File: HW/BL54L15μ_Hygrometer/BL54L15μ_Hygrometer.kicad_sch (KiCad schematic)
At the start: 20 parts, among them IC1 nrf54L 453-00223R, J1 Conn_Qwiic, J2 Conn_ARM_JTAG_SWD_10, J3 Conn_01x10_Pin, J4 Conn_01x10_Pin, J5 Conn_01x10_Pin, J6 Conn_01x10_Pin, U2 nPM2100-QEXX, U3 SHT4x

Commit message: nrf54L hygrometer prototype 2025v2
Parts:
- removed J3, J4, J5, J6: Conn_01x10_Pin, Connector_PinHeader_2.54mm:PinHeader_1x10_P2.54mm_Vertical, symbol Connector:Conn_01x10_Pin
- added C8, C9: 100nF, Capacitor_SMD:C_0402_1005Metric, symbol Device:C
- added U3: STCC4-D-R3, STCC4DR3, symbol STCC4-D-R3:STCC4-D-R3
- added U5: BME688, Package_LGA:Bosch_LGA-8_3x3mm_P0.8mm_ClockwisePinNumbering, symbol Sensor:BME680
- added X1: 32.768 kHz, Crystal:Crystal_SMD_2012-2Pin_2.0x1.2mm, symbol Device:Crystal
- BT1: Digikey Part Number (none) -> 36-2468-ND
- C1: value 47μF -> 22μF; Design Guidance At least 3.5 μF effective and 6.3V rating, ±20% is fine -> (none); Digikey Part Number (none) -> 1276-1274-1-ND
- C2: value 10nF -> 100nF; Design Guidance 1-100nF, at least 6.3V rating -> (none); Digikey Part Number (none) -> 490-6297-1-ND
- C3: Digikey Part Number (none) -> 1276-1192-1-ND
- C4: Digikey Part Number (none) -> 1276-1469-1-ND
- C5: value 10nF -> 100nF; Design Guideline 1-100nF, at least 6.3V rating -> (none); Digikey Part Number (none) -> 490-6297-1-ND
- C6: value 47μF -> 22μF; Design Guideline At least 3.5 μF effective and 6.3V rating, ±20% is fine. Ad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 -> (none); Digikey Part Number (none) -> 1276-1274-1-ND
- C7: Digikey Part Number (none) -> 490-6297-1-ND
- D1: Digikey Part Number (none) -> 732-4979-1-ND
- IC1: Digikey Part Number (none) -> 776-453-00223RCT-ND
- J1: Digikey Part Number (none) -> 455-SM04B-SRSS-TBCT-ND
- J2: Digikey Part Number (none) -> 1528-752-ND
- L1: Digikey Part Number (none) -> 1276-6901-1-ND
- R1: value 2K -> 100Ω; Digikey Part Number (none) -> 311-100HRCT-ND
- U1: renamed from U2; Digikey Part Number (none) -> 4823-NPM2100-QEAA-RCT-ND
- U2: renamed from U3; Digikey Part Number (none) -> 1649-SHT45-AD1F-R2CT-ND
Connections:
- net P1.14 is gone; now on net LED: IC1.18 (P1.14)
- net AVSS2: now also C8.2, C9.2, U3.3 (ADDR), U3.4 (VSS), U5.1 (GND), U5.5 (SDO), U5.7 (GND)
- net GPIO0: now also IC1.1 (P2.05); no longer IC1.8 (P1.07)
- net LED: no longer IC1.1 (P2.05)
- net VDD: now also C7.1, U2.3 (VDD)
- net VDDSW: now also C8.1, C9.1, U3.6 (VDDIO), U3.7 (VDD), U5.2 (CSB), U5.6 (VDDIO), U5.8 (VDD); no longer C7.1, U2.3 (VDD)
- net GPIO1: no longer names the net of U1.9 (GPIO1)
- net GPIO1: no longer IC1.9 (P1.03/NFC2/CLK)
- net P1.00 renamed XL1
- net XL1: now also X1.2
- net P1.02: no longer names the net of IC1.11 (P1.02/NFC1)
- net P1.04 renamed SCL2
- net SCL2: now also J1.4, U3.1 (SCL), U5.4 (SCK)
- net P1.05 renamed SDA2
- net SDA2: now also J1.3, U3.5 (SDA), U5.3 (SDI)
- net P1.08: no longer names the net of IC1.3 (P1.08/EXTREF/CLK16M/CLK)
- net P1.10: no longer names the net of IC1.21 (P1.10)
- net P1.11: no longer names the net of IC1.23 (P1.11/AIN4/CLK)
- net P1.12: no longer names the net of IC1.19 (P1.12/AIN5/CLK)
- net P2.00 renamed SDA1
- net SDA1: now also U1.6 (SDA), U2.1 (SDA)
- net P2.04: no longer names the net of IC1.45 (P2.04)
- net P2.06 renamed SCL1
- net SCL1: now also U1.7 (SCL), U2.2 (SCL)
- net P2.10: no longer names the net of IC1.41 (P2.10)
- net PG/RESET: no longer names the net of U1.10 (PG/RESET)
- net PG/RESET: no longer IC1.10 (P1.01/XL2)
- removed net SCL: IC1.6 (P2.01/CLK), J1.4, U1.7 (SCL), U2.2 (SCL)
- removed net SDA: IC1.7 (P1.06), J1.3, U1.6 (SDA), U2.1 (SDA)
- net SHPHELD: no longer names the net of U1.4 (SHPHLD)
- net SYSGDEN: no longer names the net of U1.8 (SYSGDEN)
- new net XL2: IC1.10 (P1.01/XL2), X1.1
- no-connect marks 15 -> 31
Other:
- note added: "ARM SWD 10-pin header"
- note added: "BL54L15μ (nrf54L15 module)"
- note added: "CO2 STCC4"
- note added: "Humidity/Temperature SHT4X"
- note added: "I2C Address = 0x64 VDD = 2.7 V - 5.5 V 1 μA sleep, 55 μA idle, 3.7 mA peak Accuracy: ±(100 ppm + 10%) (when SHT4x calibrated) 10 year lifetime"
- note added: "I2C Address: 0x44 VDD: 1.08 V - 3.6 V 0.08 μA idle, 320 μA sense, 6-100 mA heat %RH Accuracy: SHT40-43 ±1.8, SHT45 ±1.0 °C Accuracy: SHT40-43 ±0.2, SHT45 ±0.1"
- note added: "I2C Address: 0x74 Vbat: 0.7 - 3.4 V, automatic passthrough Vout: 3V initial (NC Vset), adjustable target 1.8-3.3 V 150 mA boost, 50 mA LDO/switch max output Boost efficiency 87-95% 175 nA hibernate, 35 nA ship mode Fuel gauge, boot watchdog, ADC for VBAT/VOUT/temp"
- note added: "I2C Address: 0x76 VDD: 1.71 V - 3.6 V 0.29 μA idle, 714 μA typ pressure, 12 mA typ gas"
- note added: "Non-rechargable Battery PMIC npm2100"
- note added: "Pressure/Gas BME688"
- note added: "Qwicc I2C Connector"
- note added: "Status LED"
- moved on the sheet: BT1, C1, C2, C3, C4, C5, C6, C7, D1, IC1, J1, J2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

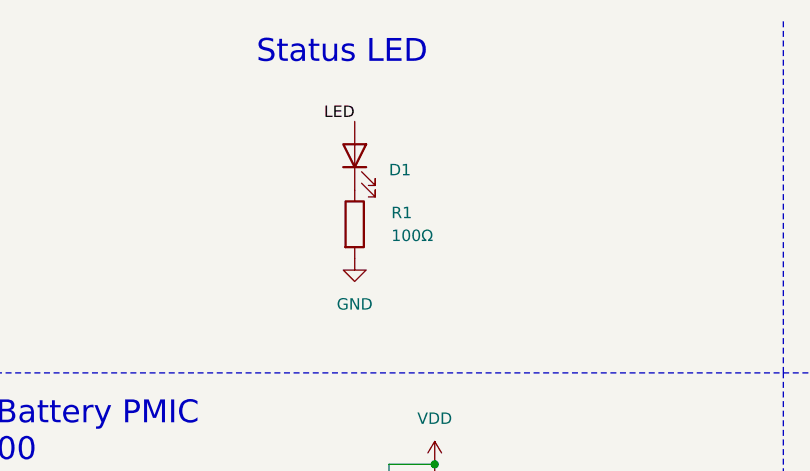
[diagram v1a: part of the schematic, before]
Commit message: Updated BOMs
No PCB changes, just adding Part Number attributes and exporting a table.

Does sneak in a corrected XTAL footprint, but it's not actually applied yet.
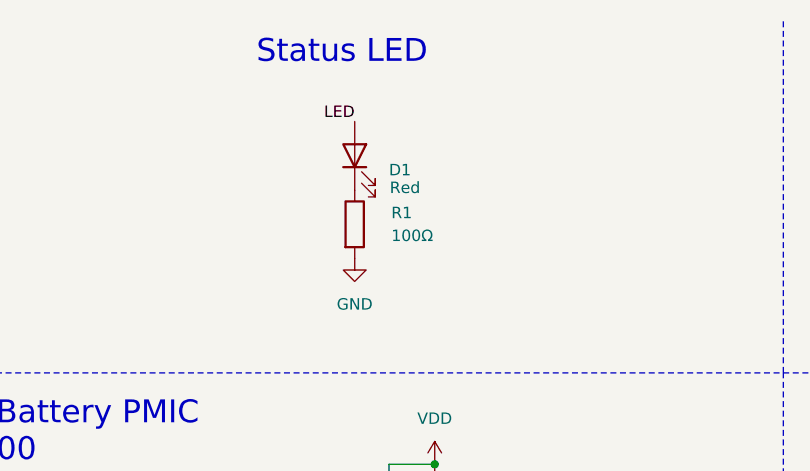
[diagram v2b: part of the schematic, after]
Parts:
- C1, C6: Digikey Part Number 1276-1274-1-ND -> (none); Part Number (none) -> CL10A226MP8NUNE
- C2, C5, C7, C8, C9: Digikey Part Number 490-6297-1-ND -> (none); Part Number (none) -> GRM155R61A104KA01J
- C3: Digikey Part Number 1276-1192-1-ND -> (none); Part Number (none) -> CL10A106KP8NNNC
- C4: Digikey Part Number 1276-1469-1-ND -> (none); Part Number (none) -> CL05A225KP5NSNC
- D1: Color (none) -> Red; Part Number (none) -> 150060SS75000
- IC1: Manufacturer_Part_Number 453-00223R -> (none); Part Number (none) -> 453-00223R
- J1: Part Number (none) -> SM04B-SRSS-TB
- L1: Part Number (none) -> CIGT201610EH2R2MNE
- R1: Digikey Part Number 311-100HRCT-ND -> (none); Part Number (none) -> RC0603FR-07100RL
- U1: Digikey Part Number 4823-NPM2100-QEAA-RCT-ND -> (none); Part Number (none) -> NPM2100-QEAA-R
- U2: Digikey Part Number 1649-SHT45-AD1F-R2CT-ND -> (none); Part Number (none) -> SHT45-AD1F-R2
- U3: Manufacturer_Part_Number STCC4-D-R3 -> (none); Part Number (none) -> STCC4-D-R3
- U5: Digikey Part Number 828-BME688CT-ND -> (none); Part Number (none) -> BME688
- X1: footprint Crystal:Crystal_SMD_2012-2Pin_2.0x1.2mm -> CM7V_T1A_LOW_ESR_32_768KHZ_9PF_20_TA_QC:XTAL_CM7V-T1A-LOW-ESR-32.768KHZ-9PF-20-TA-QC; Part Number (none) -> CM7V-T1A-LOW-ESR-32.768KHZ-9PF-20-TA-QC
